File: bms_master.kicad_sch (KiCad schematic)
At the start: 67 parts, among them J1 Conn_01x08, J2 I2C1, J3 I2C2, J4 Conn_01x05, J5 Conn_01x05, J6 SWD, SW1 SW_Push, U1 TPS7B88, U2 MCP1700x-330xxMB, U3 STM32F103C8Tx, U4 SN65HVD1050D, U5 M24C64-R, U6 MAX6126, U7 MAX11163, U8 741G3157, Y1 8M

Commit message: schematic: Assign most footprints
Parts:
- C1: footprint (none) -> Capacitor_SMD:CP_Elec_6.3x7.7
- C12, C15, C16, C17, C18, C19, C2, C20, C21, C23, C24, C3, C4: footprint (none) -> Capacitor_SMD:C_0603_1608Metric
- C22: footprint (none) -> Capacitor_SMD:C_1206_3216Metric
- D1: footprint (none) -> LED_SMD:LED_0603_1608Metric
- D4: footprint (none) -> Diode_SMD:D_SOD-323
- F1: footprint (none) -> Capacitor_SMD:C_0805_2012Metric
- J4, J5: footprint (none) -> Connector_JST:JST_PH_S5B-PH-K_1x05_P2.00mm_Horizontal
- R1, R10, R11, R12, R13, R14, R15, R16, R3, R4, R5, R6, R7, R8, R9: footprint (none) -> Resistor_SMD:R_0603_1608Metric
- TP1, TP2, TP3, TP4, TP5: footprint (none) -> TestPoint:TestPoint_Keystone_5000-5004_Miniature
- U5, U6: footprint (none) -> Package_SO:SOIC-8_3.9x4.9mm_P1.27mm
- U7: footprint (none) -> Package_SO:MSOP-10_3x3mm_P0.5mm
- U8: footprint (none) -> Package_TO_SOT_SMD:SOT-363_SC-70-6
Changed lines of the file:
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@@
 			)
 		)
-		(property "Footprint" ""
+		(property "Footprint" "TestPoint:TestPoint_Keystone_5000-5004_Miniature"
 			(at 186.69 154.94 0)
 			(effects
@@
 			)
 		)
-		(property "Footprint" ""
+		(property "Footprint" "Capacitor_SMD:C_0603_1608Metric"
 			(at 69.85 160.02 0)
 			(effects
@@
 			)
 		)
-		(property "Footprint" ""
+		(property "Footprint" "Resistor_SMD:R_0603_1608Metric"
 			(at 179.07 91.44 0)
 			(effects
@@
 			)
 		)
-		(property "Footprint" ""
+		(property "Footprint" "Diode_SMD:D_SOD-323"
 			(at 256.54 45.72 90)
 			(effects
@@
 			)
 		)
-		(property "Footprint" ""
+		(property "Footprint" "Package_TO_SOT_SMD:SOT-363_SC-70-6"
 			(at 127 78.74 0)
 			(effects
@@
 			)
 		)
-		(property "Footprint" ""
+		(property "Footprint" "Capacitor_SMD:C_0603_1608Metric"
 			(at 59.69 85.09 0)
 			(effects
@@
 			)
 		)
-		(property "Footprint" ""
+		(property "Footprint" "TestPoint:TestPoint_Keystone_5000-5004_Miniature"
 			(at 127 33.02 0)
 			(effects
@@
 			)
 		)
-		(property "Footprint" ""
+		(property "Footprint" "TestPoint:TestPoint_Keystone_5000-5004_Miniature"
 			(at 92.71 33.02 0)
 			(effects
@@
 			)
 		)
-		(property "Footprint" ""
+		(property "Footprint" "Resistor_SMD:R_0603_1608Metric"
 			(at 142.24 43.18 0)
 			(effects
@@
 			)
 		)
-		(property "Footprint" ""
+		(property "Footprint" "Package_SO:MSOP-10_3x3mm_P0.5mm"
 			(at 63.5 73.66 0)
 			(effects
@@
 			)
 		)
-		(property "Footprint" ""
+		(property "Footprint" "Capacitor_SMD:CP_Elec_6.3x7.7"
 			(at 53.34 39.37 0)
 			(effects
@@
 			)
 		)
-		(property "Footprint" ""
+		(property "Footprint" "Resistor_SMD:R_0603_1608Metric"
 			(at 260.35 38.1 0)
 			(effects
@@
 			)
 		)
-		(property "Footprint" ""
+		(property "Footprint" "Package_SO:SOIC-8_3.9x4.9mm_P1.27mm"
 			(at 10.16 87.63 0)
 			(effects
@@
 			)
 		)
-		(property "Footprint" ""
+		(property "Footprint" "Capacitor_SMD:C_0603_1608Metric"
 			(at 121.92 147.32 0)
 			(effects
@@
 			)
 		)
-		(property "Footprint" ""
+		(property "Footprint" "TestPoint:TestPoint_Keystone_5000-5004_Miniature"
 			(at 36.83 146.05 0)
 			(effects
@@
 			)
 		)
-		(property "Footprint" ""
+		(property "Footprint" "Capacitor_SMD:C_0603_1608Metric"
 			(at 74.93 160.02 0)
 			(effects
@@
 			)
 		)
-		(property "Footprint" ""
+		(property "Footprint" "Resistor_SMD:R_0603_1608Metric"
 			(at 113.03 83.82 0)
 			(effects
@@
 			)
 		)
-		(property "Footprint" ""
+		(property "Footprint" "Resistor_SMD:R_0603_1608Metric"
 			(at 147.32 43.18 0)
 			(effects
@@
 			)
 		)
-		(property "Footprint" ""
+		(property "Footprint" "Resistor_SMD:R_0603_1608Metric"
 			(at 123.19 91.44 0)
 			(effects
@@
 			)
 		)
-		(property "Footprint" ""
+		(property "Footprint" "Capacitor_SMD:C_0603_1608Metric"
 			(at 115.57 38.1 0)
 			(effects
@@
 			)
 		)
-		(property "Footprint" ""
+		(property "Footprint" "Capacitor_SMD:C_1206_3216Metric"
 			(at 50.8 85.09 0)
 			(effects
@@
 			)
 		)
-		(property "Footprint" ""
+		(property "Footprint" "Capacitor_SMD:C_0603_1608Metric"
 			(at 27.94 85.09 0)
 			(effects
@@
 			)
 		)
-		(property "Footprint" ""
+		(property "Footprint" "Capacitor_SMD:C_0603_1608Metric"
 			(at 83.82 106.68 0)
 			(effects
@@
 			)
 		)
-		(property "Footprint" ""
+		(property "Footprint" "Resistor_SMD:R_0603_1608Metric"
 			(at 153.67 43.18 0)
 			(effects
@@
 			)
 		)
-		(property "Footprint" ""
+		(property "Footprint" "Resistor_SMD:R_0603_1608Metric"
 			(at 80.01 146.05 0)
 			(effects
@@
 			)
 		)
-		(property "Footprint" ""
+		(property "Footprint" "Connector_JST:JST_PH_S5B-PH-K_1x05_P2.00mm_Horizontal"
 			(at 257.81 146.05 0)
 			(effects
@@
 			)
 		)
-		(property "Footprint" ""
+		(property "Footprint" "Capacitor_SMD:C_0603_1608Metric"
 			(at 267.97 45.72 0)
 			(effects
@@
 			)
 		)
-		(property "Footprint" ""
+		(property "Footprint" "Resistor_SMD:R_0603_1608Metric"
 			(at 153.67 153.67 0)
 			(effects
@@
 			)
 		)
-		(property "Footprint" ""
+		(property "Footprint" "Resistor_SMD:R_0603_1608Metric"
 			(at 260.35 45.72 0)
 			(effects
@@
 			)
 		)
-		(property "Footprint" ""
+		(property "Footprint" "Capacitor_SMD:C_0603_1608Metric"
 			(at 92.71 106.68 0)
 			(effects
@@
 			)
 		)
-		(property "Footprint" ""
+		(property "Footprint" "Resistor_SMD:R_0603_1608Metric"
 			(at 173.99 91.44 0)
 			(effects
@@
 			)
 		)
-		(property "Footprint" ""
+		(property "Footprint" "Capacitor_SMD:C_0603_1608Metric"
 			(at 102.87 87.63 0)
 			(effects
@@
 			)
 		)
-		(property "Footprint" ""
+		(property "Footprint" "Capacitor_SMD:C_0805_2012Metric"
 			(at 40.64 33.02 0)
 			(effects
@@
 			)
 		)
-		(property "Footprint" ""
+		(property "Footprint" "Resistor_SMD:R_0603_1608Metric"
 			(at 264.16 135.89 0)
 			(effects
@@
 			)
 		)
-		(property "Footprint" ""
+		(property "Footprint" "LED_SMD:LED_0603_1608Metric"
 			(at 27.94 38.1 90)
 			(effects
@@
 			)
 		)
-		(property "Footprint" ""
+		(property "Footprint" "Capacitor_SMD:C_0603_1608Metric"
 			(at 78.74 106.68 0)
 			(effects
@@
 			)
 		)
-		(property "Footprint" ""
+		(property "Footprint" "Resistor_SMD:R_0603_1608Metric"
 			(at 27.94 44.45 0)
 			(effects
@@
 			)
 		)
-		(property "Footprint" ""
+		(property "Footprint" "Resistor_SMD:R_0603_1608Metric"
 			(at 135.89 43.18 0)
 			(effects
@@
 			)
 		)
-		(property "Footprint" ""
+		(property "Footprint" "Resistor_SMD:R_0603_1608Metric"
 			(at 241.3 135.89 0)
 			(effects
@@
 			)
 		)
-		(property "Footprint" ""
+		(property "Footprint" "Connector_JST:JST_PH_S5B-PH-K_1x05_P2.00mm_Horizontal"
 			(at 234.95 146.05 0)
 			(effects
@@
 			)
 		)
-		(property "Footprint" ""
+		(property "Footprint" "Capacitor_SMD:C_0603_1608Metric"
 			(at 87.63 38.1 0)
 			(effects
@@
 			)
 		)
-		(property "Footprint" ""
+		(property "Footprint" "TestPoint:TestPoint_Keystone_5000-5004_Miniature"
 			(at 41.91 146.05 0)
 			(effects
@@
 			)
 		)
-		(property "Footprint" ""
+		(property "Footprint" "Package_SO:SOIC-8_3.9x4.9mm_P1.27mm"
 			(at 132.08 139.7 0)
 			(effects
@@
 			)
 		)
-		(property "Footprint" ""
+		(property "Footprint" "Capacitor_SMD:C_0603_1608Metric"
 			(at 81.28 38.1 0)
 			(effects

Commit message: schematic: Fill in most BOM info
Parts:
- C1: Dist (none) -> LCSC; Dist # (none) -> C344075; Mfr (none) -> Panasonic; Mfr # (none) -> EEEFK1J220XP
- C12, C17, C18, C19, C2, C20, C21, C24, C3, C4: Dist (none) -> LCSC; Dist # (none) -> C5199872; Mfr (none) -> Samsung; Mfr # (none) -> CL10B105KB8NQNC
- C22: Dist (none) -> LCSC; Dist # (none) -> C97954; Mfr (none) -> Murata; Mfr # (none) -> GRM31CR71C106KA12L
- C23: Dist (none) -> LCSC; Dist # (none) -> C1591; Mfr (none) -> Samsung; Mfr # (none) -> CL10B104KB8NNNC
- D1: Dist (none) -> LCSC; Dist # (none) -> C84263; Mfr (none) -> Foshan NationStar Optoelectronics; Mfr # (none) -> NCD0603R1
- D2: Dist (none) -> LCSC; Dist # (none) -> C2836396; Mfr (none) -> MSKSEMI; Mfr # (none) -> SS34-MS
- D5: Dist (none) -> LCSC; Dist # (none) -> C75176; Mfr (none) -> Nexperia; Mfr # (none) -> PESD2CAN,215
- F1: Dist (none) -> LCSC; Dist # (none) -> C207019; Mfr (none) -> Littelfuse; Mfr # (none) -> 0805L010/24YR
- J2: value I2C1 -> I2C
- J3: value I2C2 -> I2C
- J4, J5: value Conn_01x05 -> CSENSE; Dist (none) -> LCSC; Dist # (none) -> C157923; Mfr (none) -> JST; Mfr # (none) -> S5B-PH-K-S(LF)(SN)
- J6: Dist (none) -> LCSC; Dist # (none) -> C6332200; Mfr (none) -> Hanbo Electronic; Mfr # (none) -> HB-PH3-25417PB2GOP
- R1, R6: Dist (none) -> LCSC; Dist # (none) -> C25804; Mfr (none) -> Uni-Royal; Mfr # (none) -> 0603WAF1002T5E
- R10, R7, R8, R9: Dist (none) -> LCSC; Dist # (none) -> C4211; Mfr (none) -> Uni-Royal; Mfr # (none) -> 0603WAF3001T5E
- R12, R13, R14, R15, R3, R4: Dist (none) -> LCSC; Dist # (none) -> C25803; Mfr (none) -> Uni-Royal; Mfr # (none) -> 0603WAF1003T5E
- R16: Dist (none) -> LCSC; Dist # (none) -> C21190; Mfr (none) -> Uni-Royal; Mfr # (none) -> 0603WAF1001T5E
- U1: Dist (none) -> Mouser; Dist # (none) -> 595-TPS7B8850QKVURQ1; Mfr (none) -> Texas Instruments; Mfr # (none) -> 595-TPS7B8850QKVURQ1
- U2: Dist (none) -> LCSC; Dist # (none) -> C632000; Mfr (none) -> Microchip Tech; Mfr # (none) -> MCP1700T-3302E/MB
- U4: Dist (none) -> LCSC; Dist # (none) -> C14019; Mfr (none) -> Texas Instruments; Mfr # (none) -> SN65HVD1050DR
- U5: Dist (none) -> LCSC; Dist # (none) -> C79988; Mfr (none) -> STMicroelectronics; Mfr # (none) -> M24C64-RMN6TP
- U6: Dist (none) -> Mouser; Dist # (none) -> 700-MAX6126BASA41; Mfr (none) -> Analog Devices; Mfr # (none) -> MAX6126BASA41+
- U7: Dist (none) -> Mouser; Dist # (none) -> 700-MAX11163EUB+; Mfr (none) -> Analog Devices; Mfr # (none) -> MAX11163EUB+
- U8: Dist (none) -> LCSC; Dist # (none) -> C38663; Mfr (none) -> Texas Instruments; Mfr # (none) -> SN74LVC1G3157DCKR

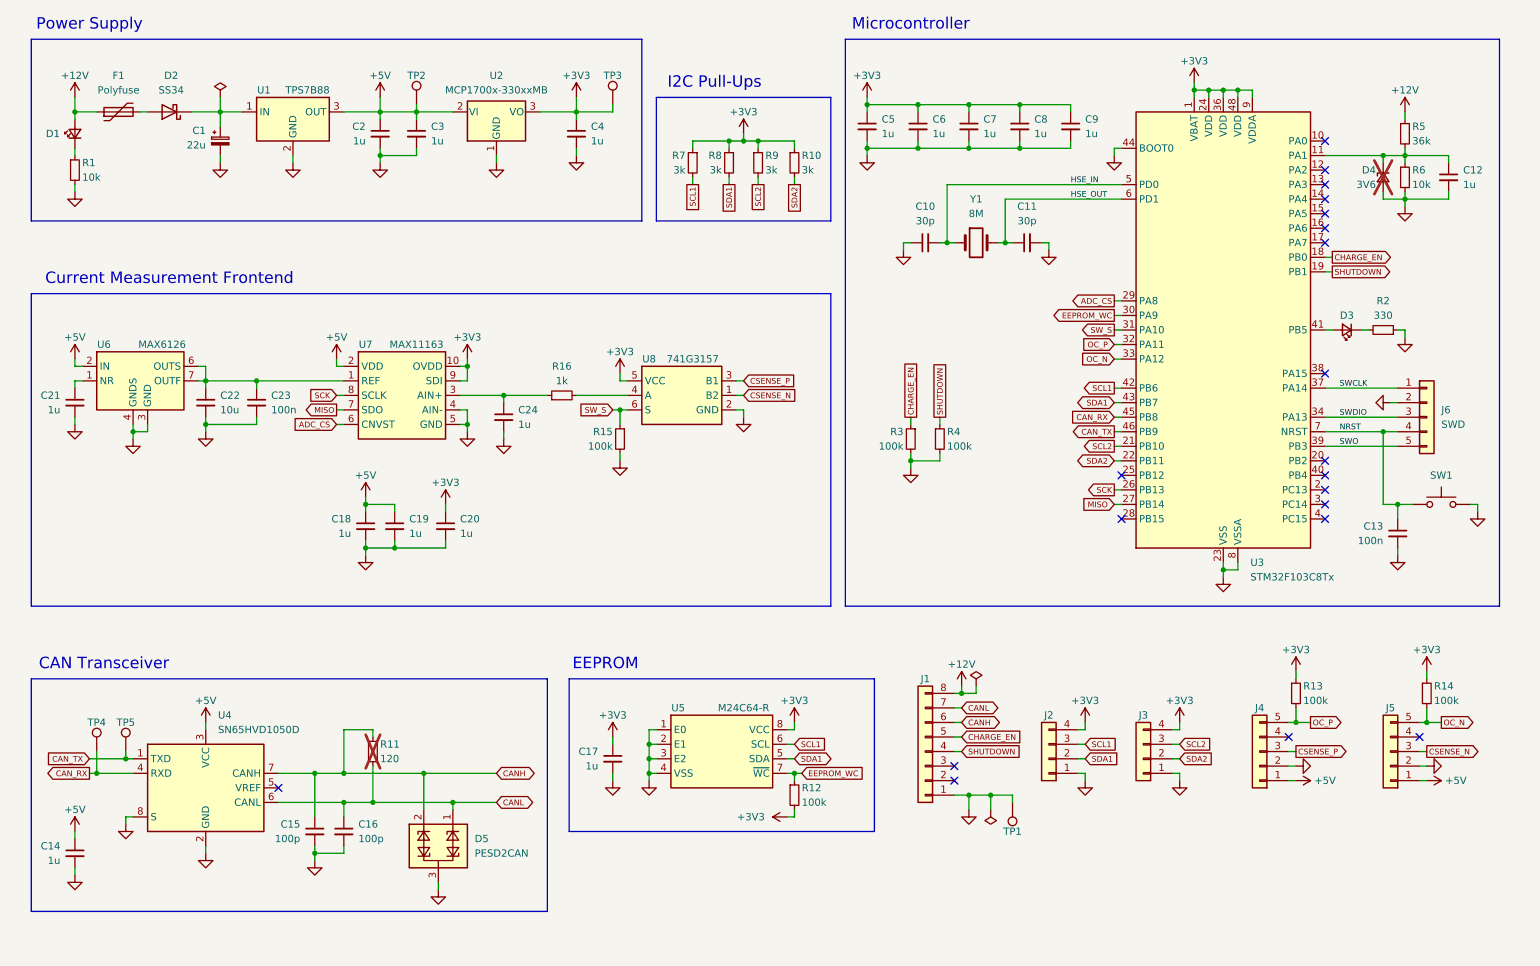
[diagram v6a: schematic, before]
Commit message: schematic: Allow powering 5V rail from SWD header
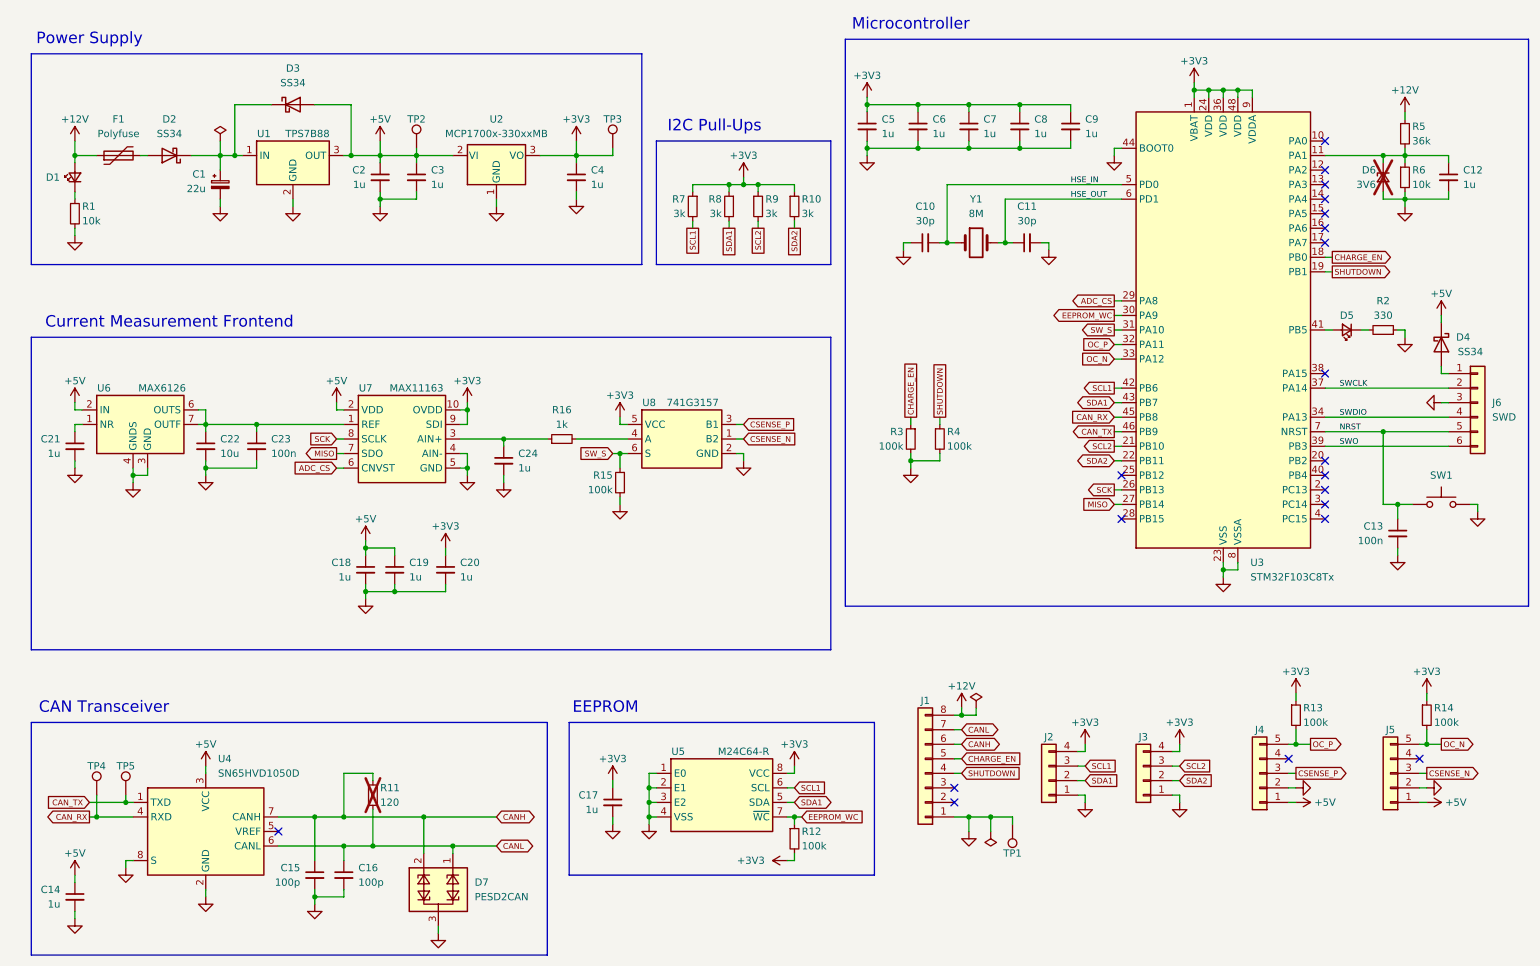
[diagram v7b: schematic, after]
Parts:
- added D3, D4: SS34, Diode_SMD:D_SMA, symbol Diode:SS34
- J6: symbol Connector_Generic:Conn_01x05 -> Connector_Generic:Conn_01x06
- renumbered D3 to D5, D4 to D6, D5 to D7
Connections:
- net +5V: now also D3.2 (A), D4.1 (K)
- net GND: now also J6.3 (Pin_3); no longer J6.2 (Pin_2)
- net NRST: now also J6.5 (Pin_5); no longer J6.4 (Pin_4)
- net SWCLK: now also J6.2 (Pin_2); no longer J6.1 (Pin_1)
- net SWDIO: now also J6.4 (Pin_4); no longer J6.3 (Pin_3)
- net SWO: now also J6.6 (Pin_6); no longer J6.5 (Pin_5)
- net at C1.1, D2.1 (K), U1.1 (IN): now also D3.1 (K)
- new net: D4.2 (A), J6.1 (Pin_1)
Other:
- moved on the sheet: C1, C14, C15, C16, C17, C18, C19, C2, C20, C21, C22, C23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

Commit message: schematic: Choose a footprint for the main connector
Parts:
- J1: footprint (none) -> Connector_Molex:Molex_Micro-Fit_3.0_43045-0812_2x04_P3.00mm_Vertical
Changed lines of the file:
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@@
 			)
 		)
-		(property "Footprint" ""
+		(property "Footprint" "Connector_Molex:Molex_Micro-Fit_3.0_43045-0812_2x04_P3.00mm_Vertical"
 			(at 176.53 149.86 0)
 			(effects
